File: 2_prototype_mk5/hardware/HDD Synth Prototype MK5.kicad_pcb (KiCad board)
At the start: 2 copper layers, 100.3 x 69.9 mm, 100 parts, among them J2 Conn_01x03, J4 USB_C_Receptacle_USB2.0_16P, J6 Conn_01x04_Pin, J7 Conn_01x05, Q1 2N7002, U1 Optocoupler_DC_PhotoNPN_AKEC, U2 MAX98357A, U3 W25Q32JVSSIQ, U4 NCP1117-3.3_SOT223, U5 RP2350_60QFN, U6 TPS63020DSJR, U7 KF350-3.5-2P, Y1 ABM8-272-T3

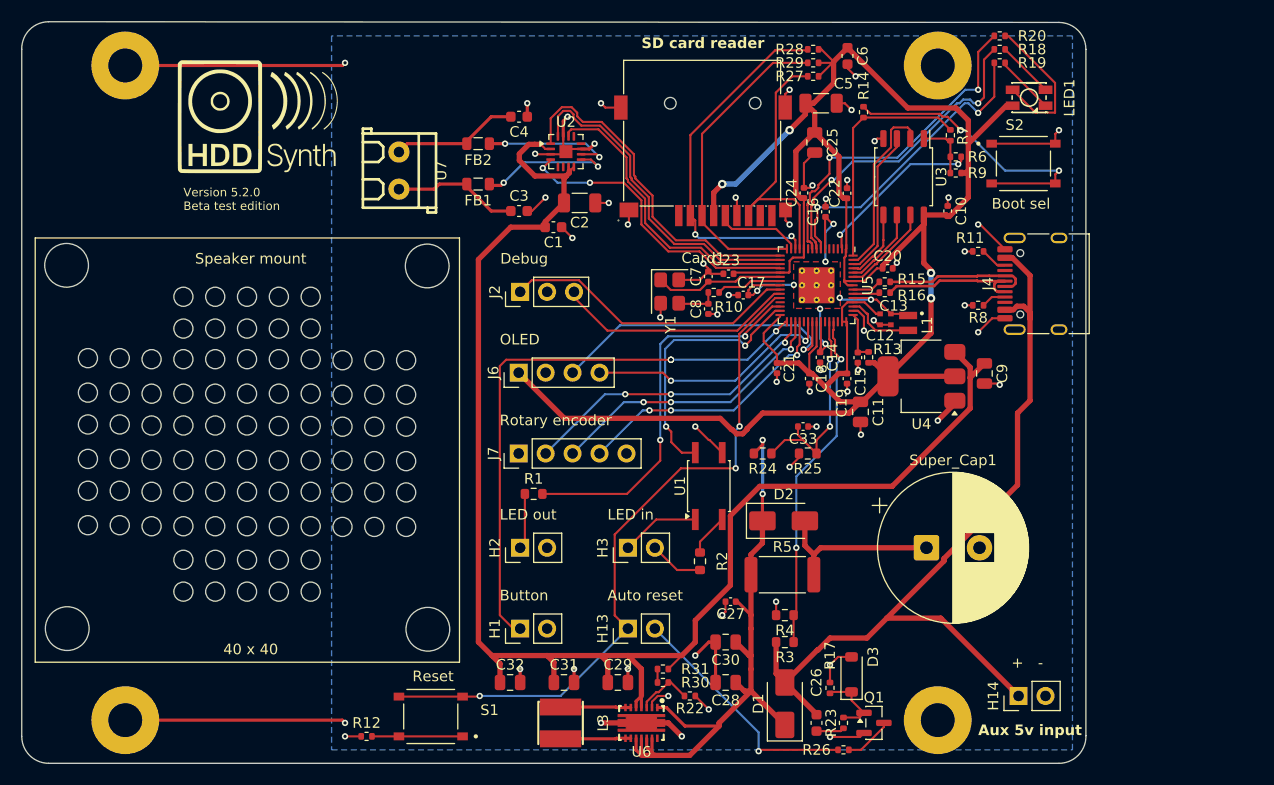
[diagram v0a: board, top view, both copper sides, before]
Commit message: Plotted most of PCB layout for eFuse and related chagnes
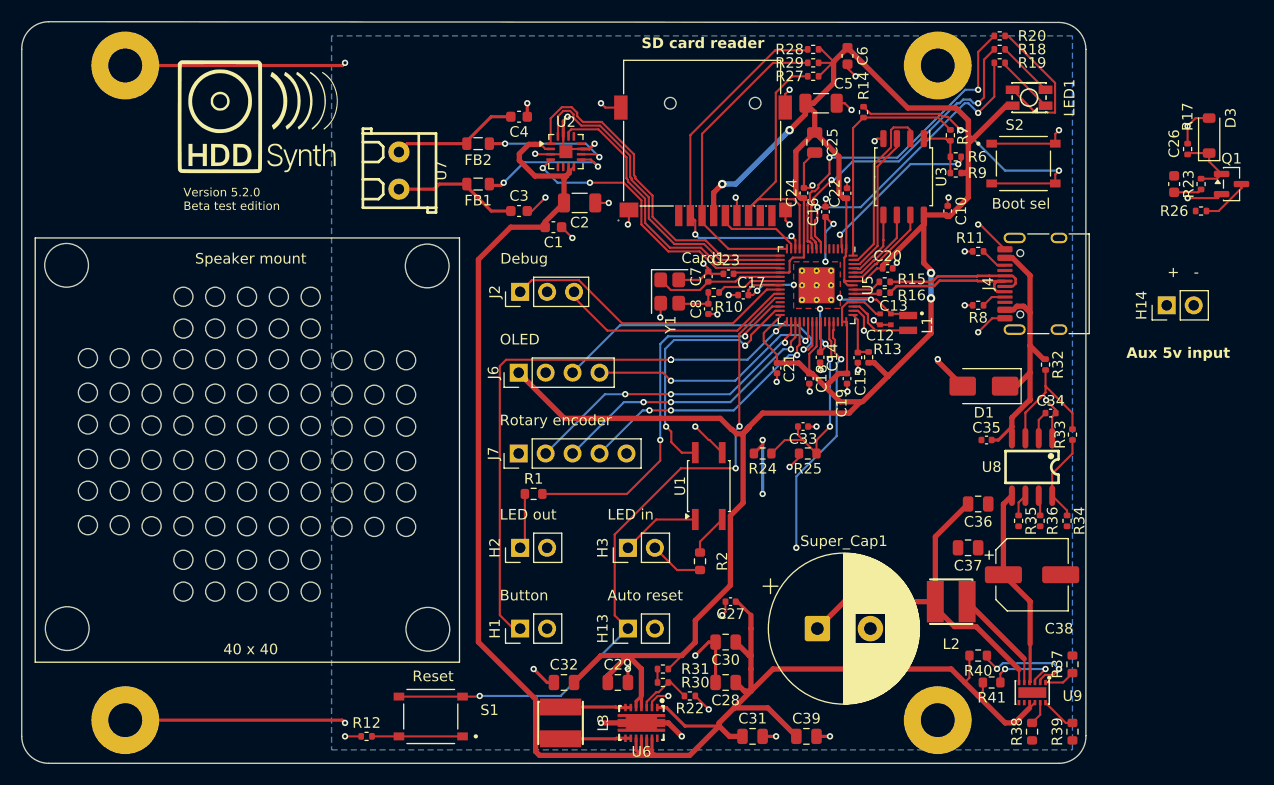
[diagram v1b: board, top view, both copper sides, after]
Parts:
- removed C11, C9: 10uF, Capacitor_SMD:C_0805_2012Metric
- removed D2: SS14, Diode_SMD:D_SMA
- removed R3, R4: 10K, Resistor_SMD:R_0603_1608Metric
- removed R5: 22R, Resistor_SMD:R_2512_6332Metric
- removed U4: NCP1117-3.3_SOT223, Package_TO_SOT_SMD:SOT-223-3_TabPin2
- added C34: 4.7nF, Capacitor_SMD:C_0402_1005Metric, F.Cu at (170.7, 83.8)
- added C35: 1uF, Capacitor_SMD:C_0402_1005Metric, F.Cu at (164.6, 86.4)
- added C36: 10uF, Capacitor_SMD:C_0805_2012Metric, F.Cu at (163.8, 92.4)
- added C37: 10uF, Capacitor_SMD:C_0805_2012Metric, F.Cu at (162.9, 96.5)
- added C38: 100uF, Capacitor_SMD:CP_Elec_6.3x7.7, F.Cu at (168.9, 99.1)
- added C39: 22uF, Capacitor_SMD:C_0805_2012Metric, F.Cu at (147.6, 114.3)
- added L2: 2.2 µH, easyeda2kicad:IND-SMD_L4.0-W4.0_FNR40XXS, F.Cu at (161.3, 101.6)
- added R32: 330K, Resistor_SMD:R_0402_1005Metric, F.Cu at (170.2, 79.2)
- added R33: 47K, Resistor_SMD:R_0402_1005Metric, F.Cu at (172.7, 85.8)
- added R34: 120K, Resistor_SMD:R_0402_1005Metric, F.Cu at (172.2, 94.0)
- added R35: 100K, Resistor_SMD:R_0402_1005Metric, F.Cu at (167.6, 94.0)
- added R36: 110K, Resistor_SMD:R_0402_1005Metric, F.Cu at (169.7, 94.0)
- added R37: 75K, Resistor_SMD:R_0603_1608Metric, F.Cu at (172.7, 107.5)
- added R38: 75K, Resistor_SMD:R_0603_1608Metric, F.Cu at (168.9, 113.9)
- added R39: 75K, Resistor_SMD:R_0603_1608Metric, F.Cu at (172.7, 113.9)
- added R40: 100K, Resistor_SMD:R_0603_1608Metric, F.Cu at (163.8, 106.7)
- added R41: 100K, Resistor_SMD:R_0603_1608Metric, F.Cu at (165.1, 109.2)
- added U8: TPS25921ADR, easyeda2kicad:SOIC-8_L5.0-W4.0-P1.27-LS6.0-BL, F.Cu at (168.9, 88.9)
- added U9: TPS61094DSSR, easyeda2kicad:WSON-12_L3.0-W2.0-P0.5-BL-EP, F.Cu at (168.9, 110.2)
- D1: value SS14 -> SMAJ5.0A
- R31: value 100K -> 24K
- Super_Cap1: value 1F -> 1.5F
- moved C26 61.0 mm to (182.3, 62.2)
- moved Q1 61.0 mm to (187.7, 62.2)
- moved R17 61.0 mm to (183.6, 58.9)
- moved R23 61.0 mm to (184.8, 62.2)
- moved D3 61.0 mm to (185.6, 57.7)
- moved R26 61.0 mm to (184.8, 64.8)
- moved H14 39.4 mm to (181.6, 73.7)
- moved D1 35.3 mm to (164.4, 81.3), turned to 180 degrees
- moved C31 18.5 mm to (142.6, 114.3)
- moved Super_Cap1 12.8 mm to (148.7, 104.1)
- moved C32 5.08 mm to (124.8, 109.2)
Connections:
- net /Power/VCAP_DETECT renamed /Power/VSUP_SENSE
- C1 pad 2: POWER_5V_SUP -> VSYS
- C2 pad 2: POWER_5V_SUP -> VSYS
- C27 pad 1: /Power/VCAP_RAW -> VSYS
- C28 pad 1: /Power/VCAP_RAW -> VSYS
- C29 pad 1: POWER_5V_SUP -> +3V3
- C30 pad 1: /Power/VCAP_RAW -> VSYS
- C31 pad 1: POWER_5V_SUP -> VSYS
- C32 pad 1: POWER_5V_SUP -> GND
- C32 pad 2: GND -> +3V3
- D1 pad 1: /Power/VCAP_RAW -> +5V
- D1 pad 2: +5V -> GND
- R24 pad 2: /Power/VCAP_RAW -> Net-(U9-SUP)
- R31 pad 1: POWER_5V_SUP -> +3V3
- Super_Cap1 pad 1: Net-(D2-A) -> Net-(U9-SUP)
- U2 pad 2: POWER_5V_SUP -> VSYS
- U2 pad 7: POWER_5V_SUP -> VSYS
- U2 pad 8: POWER_5V_SUP -> VSYS
- U5 pad 42: /Power/VCC_DETECT -> /RP2350/PWR_FAULT_N
- U6 pad 1: /Power/VCAP_RAW -> VSYS
- U6 pad 10: /Power/VCAP_RAW -> VSYS
- U6 pad 11: /Power/VCAP_RAW -> VSYS
- U6 pad 12: /Power/VCAP_RAW -> VSYS
- U6 pad 13: /Power/VCAP_RAW -> VSYS
- U6 pad 4: POWER_5V_SUP -> +3V3
- U6 pad 5: POWER_5V_SUP -> +3V3
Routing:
- net VSYS: track 0.00 -> 171.5 mm
- net POWER_5V_SUP: track 147.7 -> 0.00 mm
- net /Power/VCAP_RAW: track 62.6 -> 0.00 mm, vias 2 -> 0
- net +5V: track 80.3 -> 29.2 mm
- net Net-(U9-SUP): track 0.00 -> 43.3 mm, vias 0 -> 2
- net +3V3: track 210.9 -> 251.8 mm
- net /Power/VCC_DETECT: track 32.4 -> 0.00 mm, vias 2 -> 0
- net /RP2350/PWR_FAULT_N: track 0.00 -> 25.5 mm, vias 0 -> 2
- net Net-(H13-Pin_2): track 23.2 -> 0.00 mm, vias 1 -> 0
- net /Power/VIN_PROT: track 0.00 -> 19.0 mm
- net Net-(D2-A): track 16.3 -> 0.00 mm
- net Net-(U8-ENUV): track 0.00 -> 12.3 mm
- net Net-(U9-MODE): track 0.00 -> 10.4 mm, vias 0 -> 2
- net Net-(U9-SW): track 0.00 -> 9.85 mm
- net Net-(U8-OVP): track 0.00 -> 8.48 mm
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
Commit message: Tweaks
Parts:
- moved Q1 43.9 mm to (155.8, 92.3)
- moved D3 43.9 mm to (153.7, 87.7)
- moved R26 43.9 mm to (152.9, 94.8)
- moved R17 43.9 mm to (151.6, 89.0)
- moved R23 36.4 mm to (157.0, 85.6), turned to -90 degrees
- moved C26 33.1 mm to (156.2, 82.5)
- moved H14 21.3 mm to (161.3, 80.0)
- moved D1 8.52 mm to (160.6, 88.9)
- moved C35 1.27 mm to (163.3, 86.4)
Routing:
- net +5V: track 29.2 -> 45.2 mm
- net Net-(U9-SUP): track 43.3 -> 58.2 mm
- net GND: track 158.8 -> 155.2 mm, vias 56 -> 55
- net Net-(D3-K): track 6.66 -> 9.82 mm
- net Net-(C26-Pad1): track 2.65 -> 2.08 mm
- net /RP2350/PWR_FAULT_N: vias 2 -> 1
